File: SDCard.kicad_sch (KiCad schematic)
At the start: 1 part, among them J9 Micro_SD_Card_Det

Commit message: neatening things up
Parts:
- J9: footprint Connector_Card:microSD_HC_Hirose_DM3AT-SF-PEJM5 -> UTSVT_Connectors:microSD_HC_Hirose_DM3AT-SF-PEJM5
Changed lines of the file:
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@@
       (effects (font (size 1.27 1.27)))
     )
-    (property "Footprint" "Connector_Card:microSD_HC_Hirose_DM3AT-SF-PEJM5" (at 203.835 81.28 0)
+    (property "Footprint" "UTSVT_Connectors:microSD_HC_Hirose_DM3AT-SF-PEJM5" (at 203.835 81.28 0)
       (effects (font (size 1.27 1.27)) hide)
     )

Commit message: bom, gerbers, edge cuts, footprint verification
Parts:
- J9: P/N (none) -> DM3AT-SF-PEJM5
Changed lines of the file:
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@@
       (effects (font (size 1.27 1.27)) hide)
     )
-    (property "Datasheet" "https://www.hirose.com/product/en/download_file/key_name/DM3/category/Catalog/doc_file_id/49662/?file_category_id=4&item_id=195&is_series=1" (at 151.765 96.52 0)
+    (property "Datasheet" "https://www.mouser.com/datasheet/2/185/DM3AT_SF_PEJM5_CL0609_0031_0_00_2DDrawing_00009471-1614303.pdf" (at 151.765 96.52 0)
       (effects (font (size 1.27 1.27)) hide)
     )
+    (property "P/N" "DM3AT-SF-PEJM5" (at 151.765 99.06 0)
+      (effects (font (size 1.27 1.27)) hide)
+    )

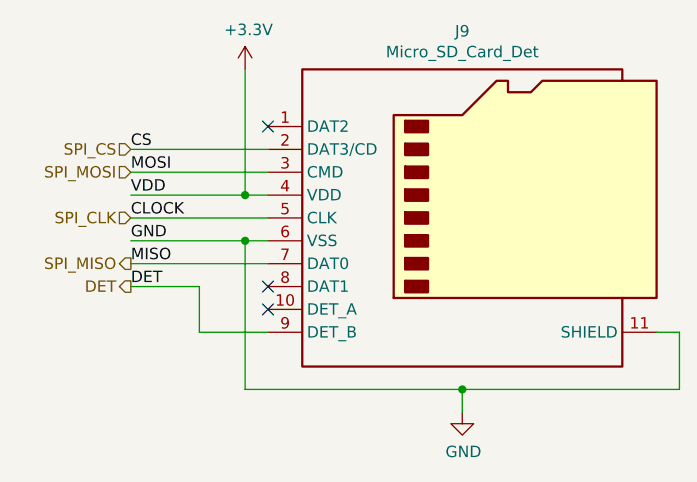
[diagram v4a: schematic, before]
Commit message: bluetooth schematic additions
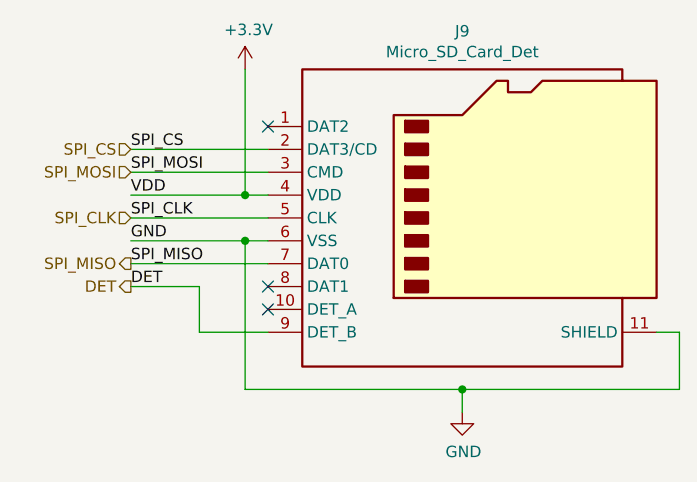
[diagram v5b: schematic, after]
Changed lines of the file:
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@@
     (stroke (width 0) (type default))
   )
-  (label "CLOCK" (at 113.665 99.06 0) (fields_autoplaced)
+  (label "SPI_CLK" (at 113.665 99.06 0) (fields_autoplaced)
     (effects (font (size 1.27 1.27)) (justify left bottom))
   )
@@
     (effects (font (size 1.27 1.27)) (justify left bottom))
   )
-  (label "CS" (at 113.665 91.44 0) (fields_autoplaced)
+  (label "SPI_CS" (at 113.665 91.44 0) (fields_autoplaced)
     (effects (font (size 1.27 1.27)) (justify left bottom))
   )
-  (label "MISO" (at 113.665 104.14 0) (fields_autoplaced)
+  (label "SPI_MISO" (at 113.665 104.14 0) (fields_autoplaced)
     (effects (font (size 1.27 1.27)) (justify left bottom))
   )
@@
     (effects (font (size 1.27 1.27)) (justify left bottom))
   )
-  (label "MOSI" (at 113.665 93.98 0) (fields_autoplaced)
+  (label "SPI_MOSI" (at 113.665 93.98 0) (fields_autoplaced)
     (effects (font (size 1.27 1.27)) (justify left bottom))
   )

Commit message: inputs routing + fixed models + clock keepouts
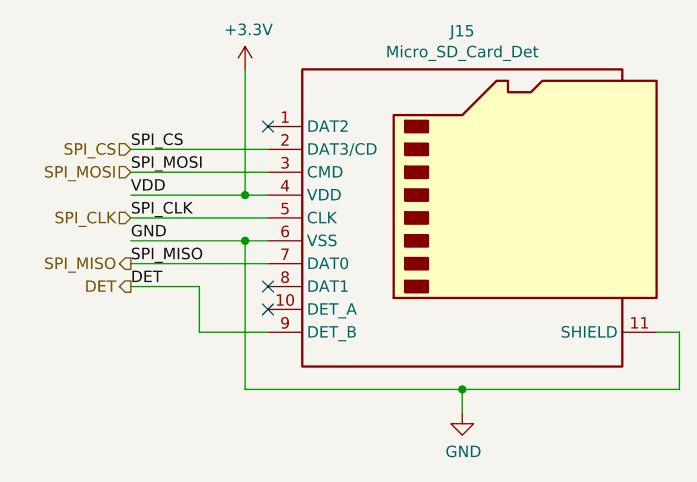
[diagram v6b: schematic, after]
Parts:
- renumbered J9 to J15
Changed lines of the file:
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@@
   (symbol (lib_id "Connector:Micro_SD_Card_Det2") (at 151.765 99.06 0) (unit 1)
     (in_bom yes) (on_board yes) (dnp no)
-    (property "Reference" "J9" (at 150.495 78.3082 0)
+    (property "Reference" "J15" (at 150.495 78.3082 0)
       (effects (font (size 1.27 1.27)))
     )
@@
       (project "Telemetry-Primary"
         (path "/7f2a449b-14af-42b3-8d38-5f0f8a5ee7ce/00000000-0000-0000-0000-00005f71644d"
-          (reference "J9") (unit 1)
+          (reference "J15") (unit 1)
         )
       )
